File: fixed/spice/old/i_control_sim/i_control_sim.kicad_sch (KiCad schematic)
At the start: 6 parts, among them Q2 MMBT3904, U1 LMV321

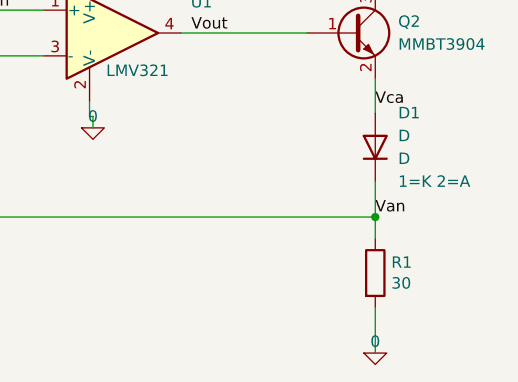
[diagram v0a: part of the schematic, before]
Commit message: Work on rev2 of fixed 25mA radial design.
Finished layout, routing and fab files.
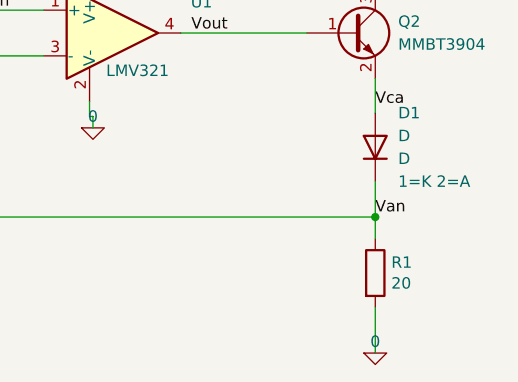
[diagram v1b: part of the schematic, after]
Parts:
- R1: value 30 -> 20
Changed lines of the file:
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@@
       (effects (font (size 1.27 1.27)) (justify left))
     )
-    (property "Value" "30" (at 171.958 92.583 0)
+    (property "Value" "20" (at 171.958 92.583 0)
       (effects (font (size 1.27 1.27)) (justify left))
     )
